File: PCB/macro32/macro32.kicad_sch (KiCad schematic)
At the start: 14 parts, among them J1 OLED, J2 OLED, J3 Magnetic connector, J4 Magnetic connector, J5 Magnetic connector, J6 Magnetic connector, SW1 RST, U1 SuperMini_NRF52840

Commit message: macro32_v2_schem&pcb
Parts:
- removed J1: OLED, KillrOfLife_Connectors:OLED_4Pin, symbol KillrOfLife:OLED-4pin
- removed J2: OLED, KillrOfLife_Connectors:OLED_5Pin, symbol KillrOfLife:OLED-5pin
- removed R1, R2: 10k, Resistor_SMD:R_0805_2012Metric_Pad1.20x1.40mm_HandSolder, symbol Device:R
- removed U1: SuperMini_NRF52840, KillrOfLife_MCU:SuperMini_NRF52850_pro_micro, symbol ScottoKeebs:MCU_SuperMini_NRF52840
- added C1, C2, C4: 1μF, Capacitor_SMD:C_0805_2012Metric_Pad1.18x1.45mm_HandSolder, symbol Device:C
- added C10, C11, C5, C6, C7, C8, C9: 100nF, Capacitor_SMD:C_0805_2012Metric_Pad1.18x1.45mm_HandSolder, symbol Device:C
- added C3: 4,7μF, Capacitor_SMD:C_0805_2012Metric_Pad1.18x1.45mm_HandSolder, symbol Device:C
- added F1: 500mA, KillrOfLife_Components:Resistor_1206, symbol Device:Polyfuse
- added J1: USB_C_Receptacle_USB2.0_16P, Connector_USB:USB_C_Receptacle_GCT_USB4110, symbol Connector:USB_C_Receptacle_USB2.0_16P
- added J2: TC2030, Connector:Tag-Connect_TC2030-IDC-FP_2x03_P1.27mm_Vertical, symbol Connector:TC2030
- added R10, R7: 10kΩ, KillrOfLife_Components:Resistor_0805, symbol Device:R
- added R5, R6: 5k1Ω, KillrOfLife_Components:Resistor_0805, symbol Device:R
- added R8, R9: 2.2kΩ, KillrOfLife_Components:Resistor_0805, symbol Device:R
- added SW2: BOOT, Button_Switch_SMD:SW_SPST_TS-1088-xR020, symbol Switch:SW_Push
- added U1: USBLC6-2P6, Package_TO_SOT_SMD:SOT-666, symbol Power_Protection:USBLC6-2P6
- added U2: STM32F072C8Tx, Package_QFP:LQFP-48_7x7mm_P0.5mm, symbol MCU_ST_STM32F0:STM32F072C8Tx
- added U3: XC6206PxxxMR, Package_TO_SOT_SMD:SOT-23-3, symbol Regulator_Linear:XC6206PxxxMR
- J3: footprint Library:fakemag4pin90degFemale -> KillrOfLife_Connectors:fakemag4pin90degFemale
- J4: renamed from J5; footprint Library:fakemag4pin90degFemale -> KillrOfLife_Connectors:fakemag4pin90degFemale
- J5: renamed from J4; footprint Library:fakemag4pin90degMale -> KillrOfLife_Connectors:fakemag4pin90degFemale
- J6: footprint Library:fakemag4pin90degMale -> KillrOfLife_Connectors:fakemag4pin90degFemale
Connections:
- net +3V3: now also C10.1, C11.1, C2.1, C3.1, C4.1, C5.1, C7.1, C8.1, C9.1, R10.2, R8.2, R9.2, SW2.1, U2.1 (VBAT), U2.24 (VDD), U2.36 (VDDIO2), U2.48 (VDD), U2.9 (VDDA), U3.2 (VO); no longer J3.1 (P1), J4.1 (P1), J5.4 (P4), J6.4 (P4)
- net COL0: now also U2.22 (PB11)
- net COL1: now also U2.21 (PB10)
- net COL2: now also U2.19 (PB1)
- net COL3: now also U2.18 (PB0)
- net COL4: now also U2.17 (PA7)
- net GND: now also C1.2, C10.2, C11.2, C2.2, C3.2, C4.2, C5.2, C6.1, C7.2, C8.2, C9.2, J1.A1 (GND), J1.A12 (GND), J1.B1 (GND), J1.B12 (GND), J1.SH (SHIELD), J2.5, R5.2, R6.2, R7.2, U1.2 (GND), U2.23 (VSS), U2.35 (VSS), U2.47 (VSS), U2.8 (VSSA), U3.1 (GND)
- net ROW0: now also U2.20 (PB2)
- net ROW1: now also U2.16 (PA6)
- net ROW2: now also U2.15 (PA5)
- net ROW3: now also U2.14 (PA4)
- net ROW4: now also U2.13 (PA3)
- net RST: now also C6.2, U2.7 (NRST)
- net SCL: now also R8.1, U2.42 (PB6); no longer J4.2 (P2), J6.3 (P3)
- net SDA: now also R9.1, U2.43 (PB7); no longer J4.3 (P3), J6.2 (P2)
- net encoder1_1: now also U2.11 (PA1)
- net encoder2_1: now also U2.12 (PA2)
- net encoders: now also U2.10 (PA0)
- new net: J1.B5 (CC2), R6.1
- new net: J1.A5 (CC1), R5.1
- new net +5V: C1.1, F1.2, J2.1, J3.1 (P1), J4.1 (P1), J5.4 (P4), J6.4 (P4), U1.5 (VBUS), U3.3 (VI)
- new net BOOT: R7.1, SW2.2, U2.44 (BOOT0)
- new net D+: J2.4, U1.6 (I/O1), U2.33 (PA12)
- new net D-: J2.3, U1.4 (I/O2), U2.32 (PA11)
- new net INT: J4.3 (P3), J6.2 (P2), R10.1, U2.45 (PB8)
- new net RX: J2.6, U2.31 (PA10)
- new net TX: J2.2, U2.30 (PA9)
- new net USB D+: J1.A6 (D+), J1.B6 (D+), U1.1 (I/O1)
- new net USB D-: J1.A7 (D-), J1.B7 (D-), U1.3 (I/O2)
- new net VBUS: F1.1, J1.A4 (VBUS), J1.A9 (VBUS), J1.B4 (VBUS), J1.B9 (VBUS)
- new net neopixel: U2.29 (PA8)
- no-connect marks 4 -> 19
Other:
- added sheet Neopixels (macro32_neopixels.kicad_sch)
- note added: "5v -> 3v3"
- note added: "Power protection"
- note added: "STM32F072"
- note added: "USB & Debug"
- note added: "USB data protection"
- note added: "Voltage regulator"
- note removed: "OLED screen"
- note removed: "Pro-micro compatible Microcontroller"
- moved on the sheet: H1, H2, H3, H4, J3, J4, J5, J6

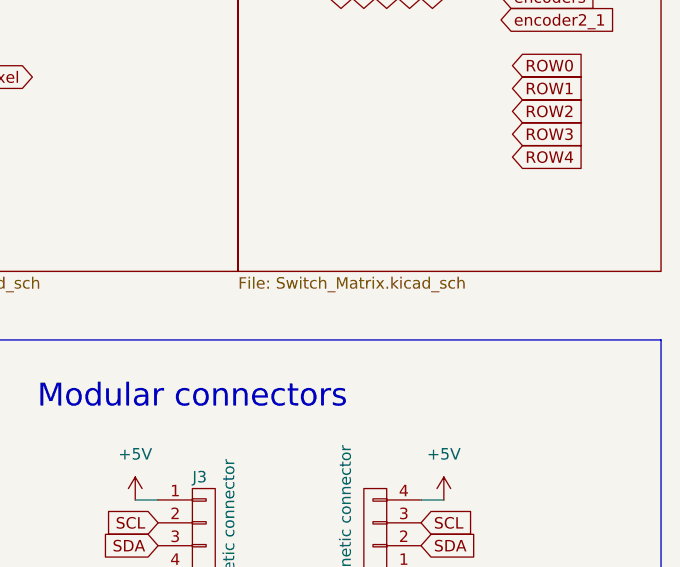
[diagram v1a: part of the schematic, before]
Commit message: fix subschema ref
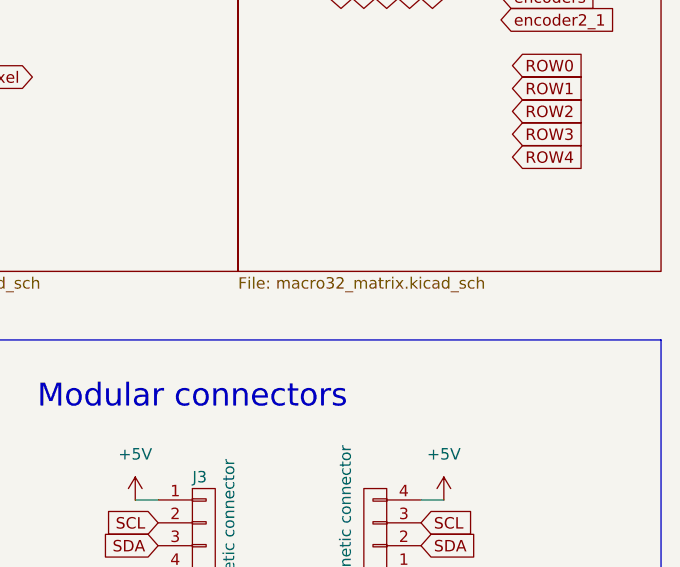
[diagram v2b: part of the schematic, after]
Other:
- sheet Switch Matrix: file Switch_Matrix.kicad_sch -> macro32_matrix.kicad_sch
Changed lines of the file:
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@@
 			)
 		)
-		(property "Sheetfile" "Switch_Matrix.kicad_sch"
+		(property "Sheetfile" "macro32_matrix.kicad_sch"
 			(at 234.95 56.4646 0)
 			(show_name no)

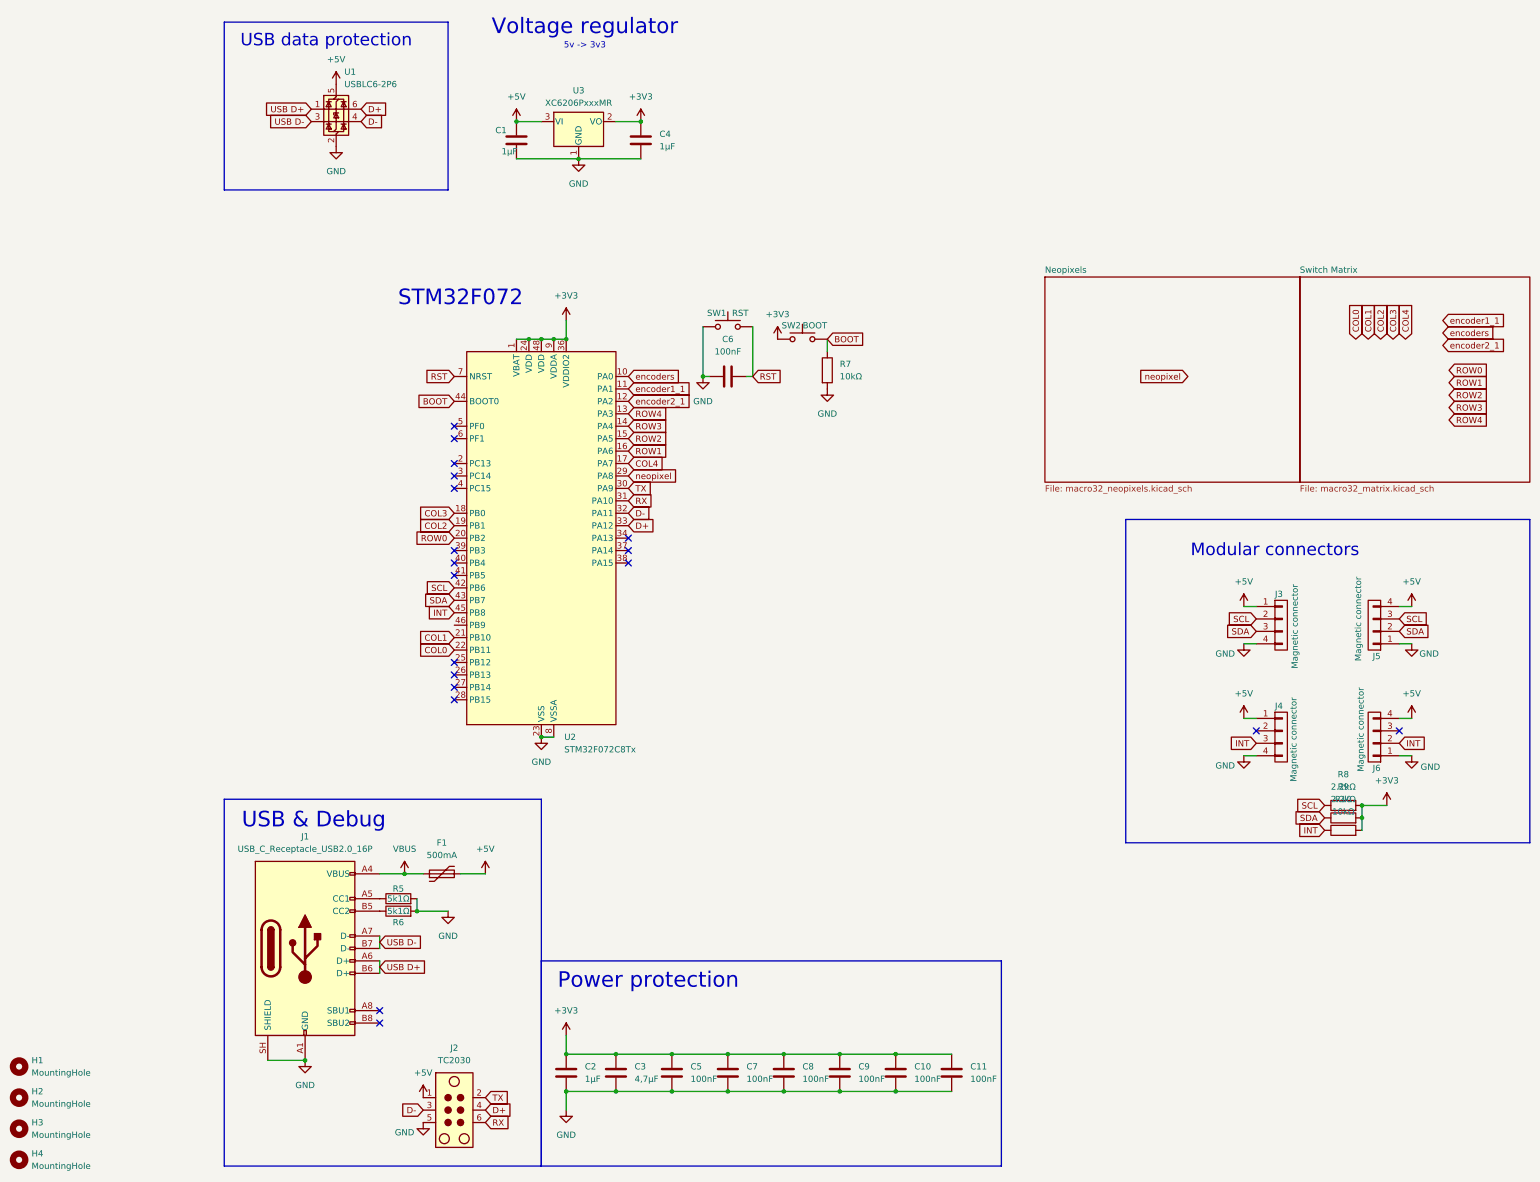
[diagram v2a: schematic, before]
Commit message: fix schema header
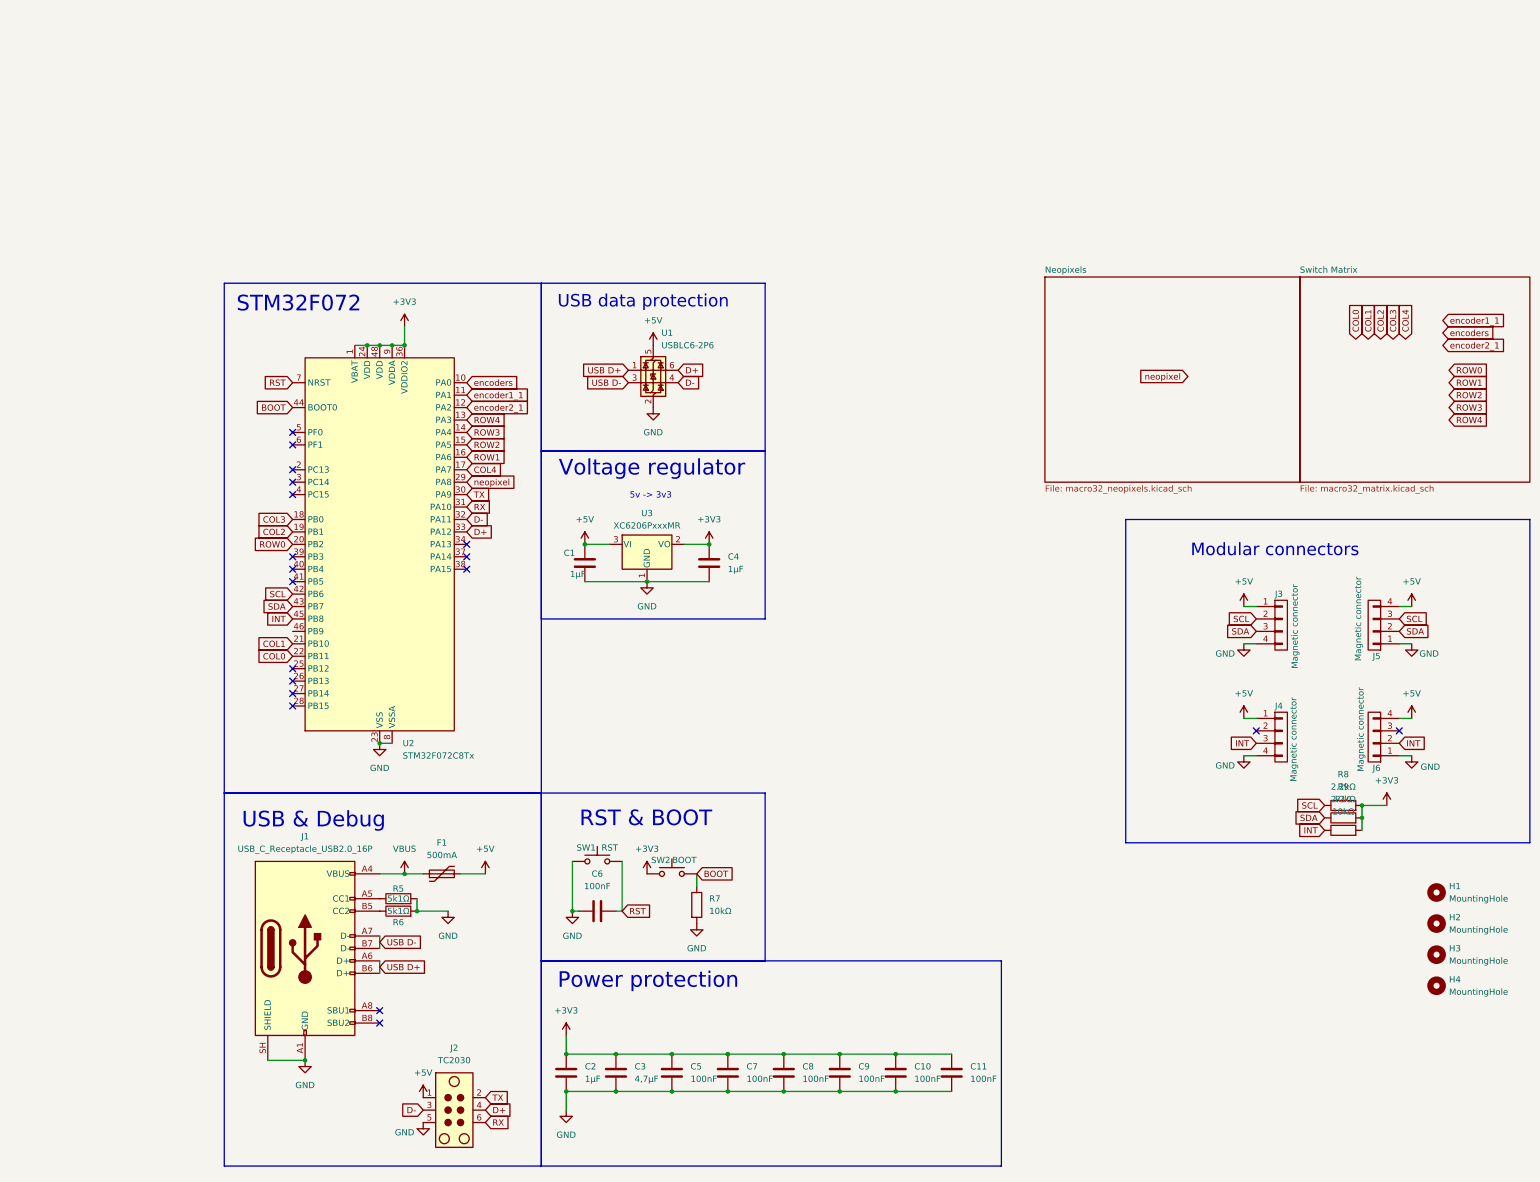
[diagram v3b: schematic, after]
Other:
- note added: "RST & BOOT"
- company: KillrOfLife -> Lucid-void
- moved on the sheet: C1, C4, C6, H1, H2, H3, H4, R7, SW1, SW2, U1, U2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

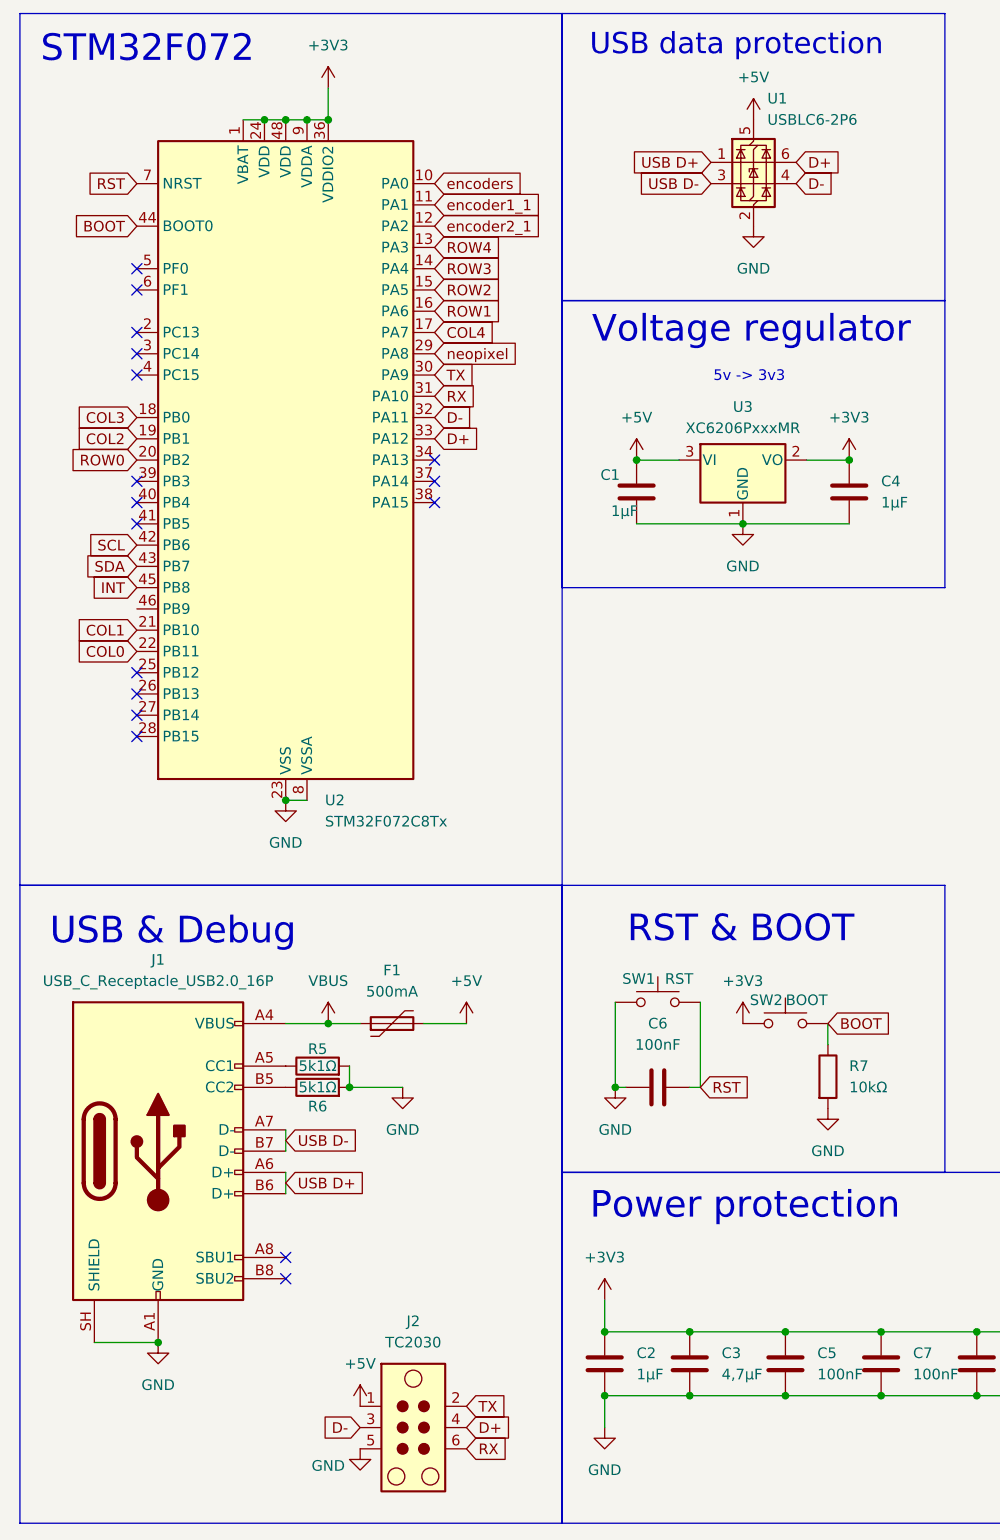
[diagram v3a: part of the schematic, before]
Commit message: redid routing reference plane for the usb data lines power in through caps
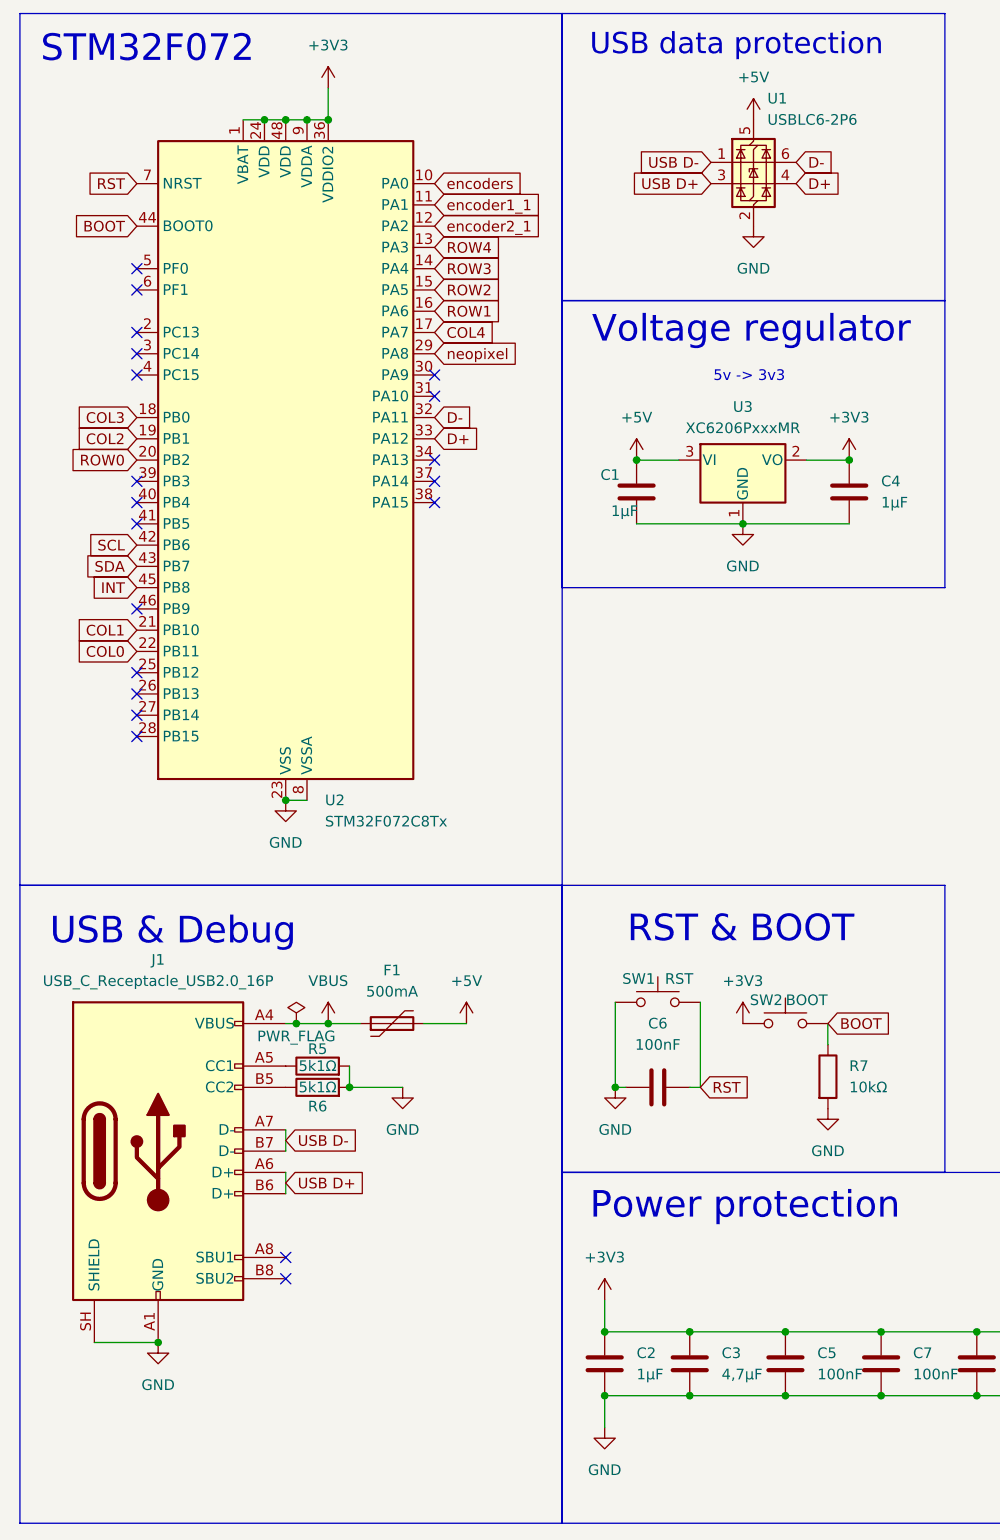
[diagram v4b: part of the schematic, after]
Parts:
- removed J2: TC2030, Connector:Tag-Connect_TC2030-IDC-FP_2x03_P1.27mm_Vertical, symbol Connector:TC2030
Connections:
- net D+: now also U1.4 (I/O2); no longer U1.6 (I/O1)
- net D-: now also U1.6 (I/O1); no longer U1.4 (I/O2)
- net USB D+: now also U1.3 (I/O2); no longer U1.1 (I/O1)
- net USB D-: now also U1.1 (I/O1); no longer U1.3 (I/O2)
- net RX: no longer names the net of U2.31 (PA10)
- net TX: no longer names the net of U2.30 (PA9)
- no-connect marks 19 -> 22
